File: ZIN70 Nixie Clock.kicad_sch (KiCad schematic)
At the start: 21 parts, among them U1 HV5122, U2 HV5122, U3 CD40109BPW

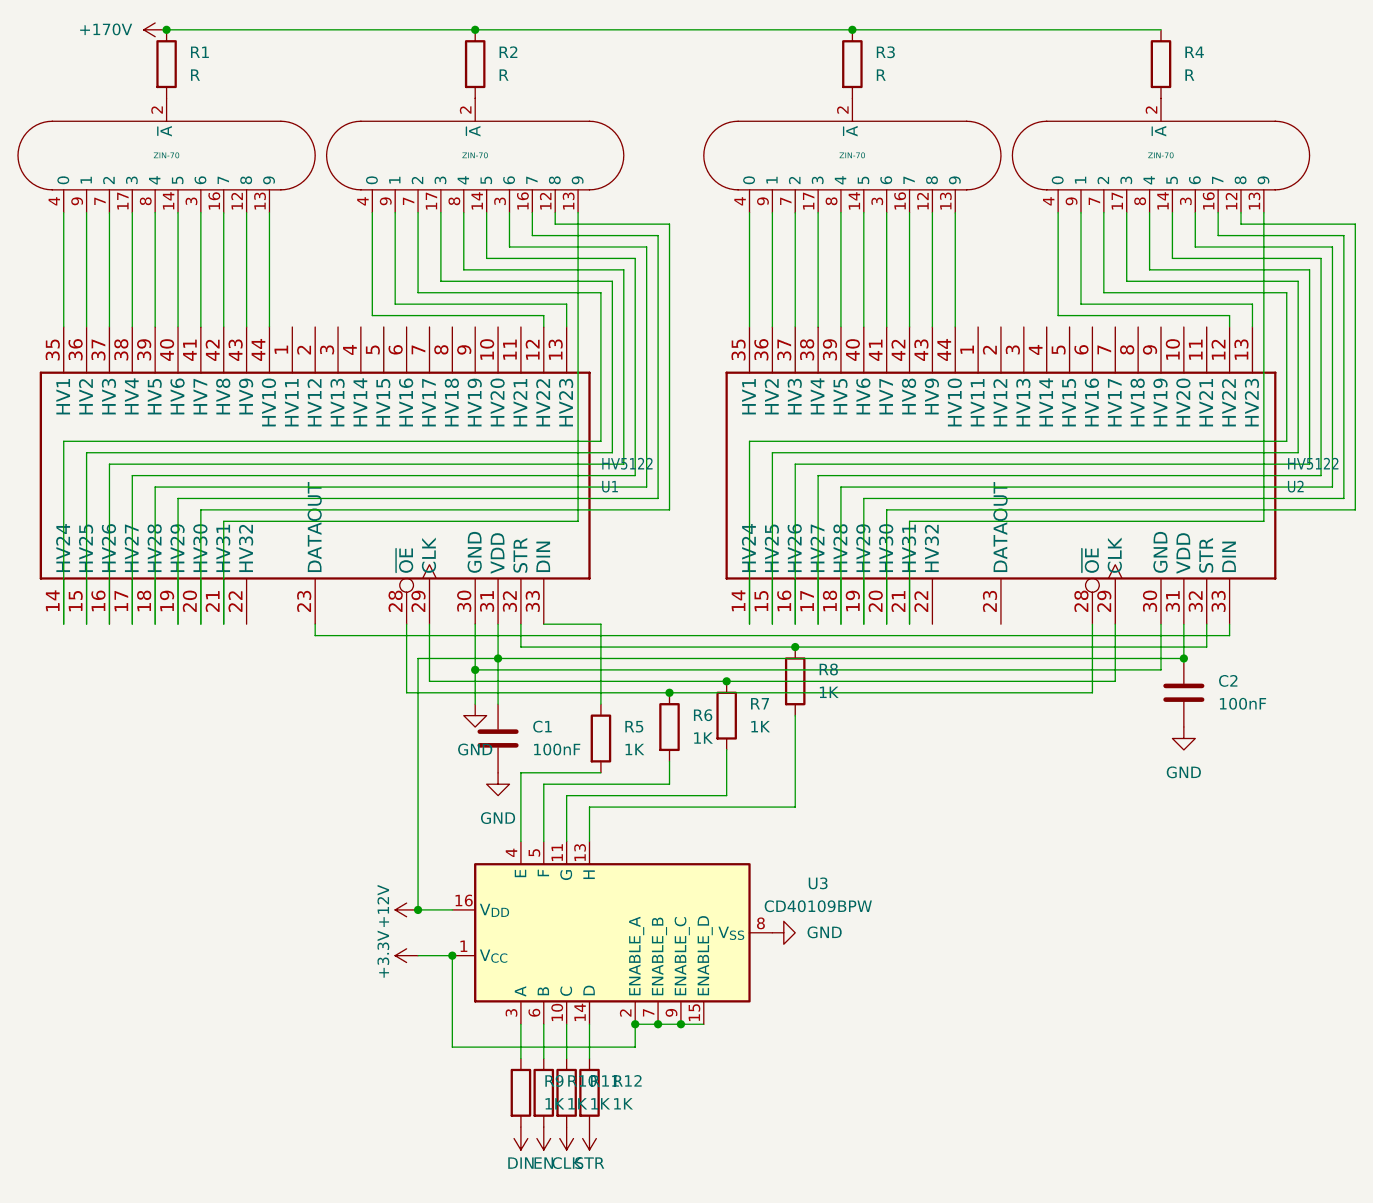
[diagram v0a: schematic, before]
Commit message: Update the clock with 5mm indicators
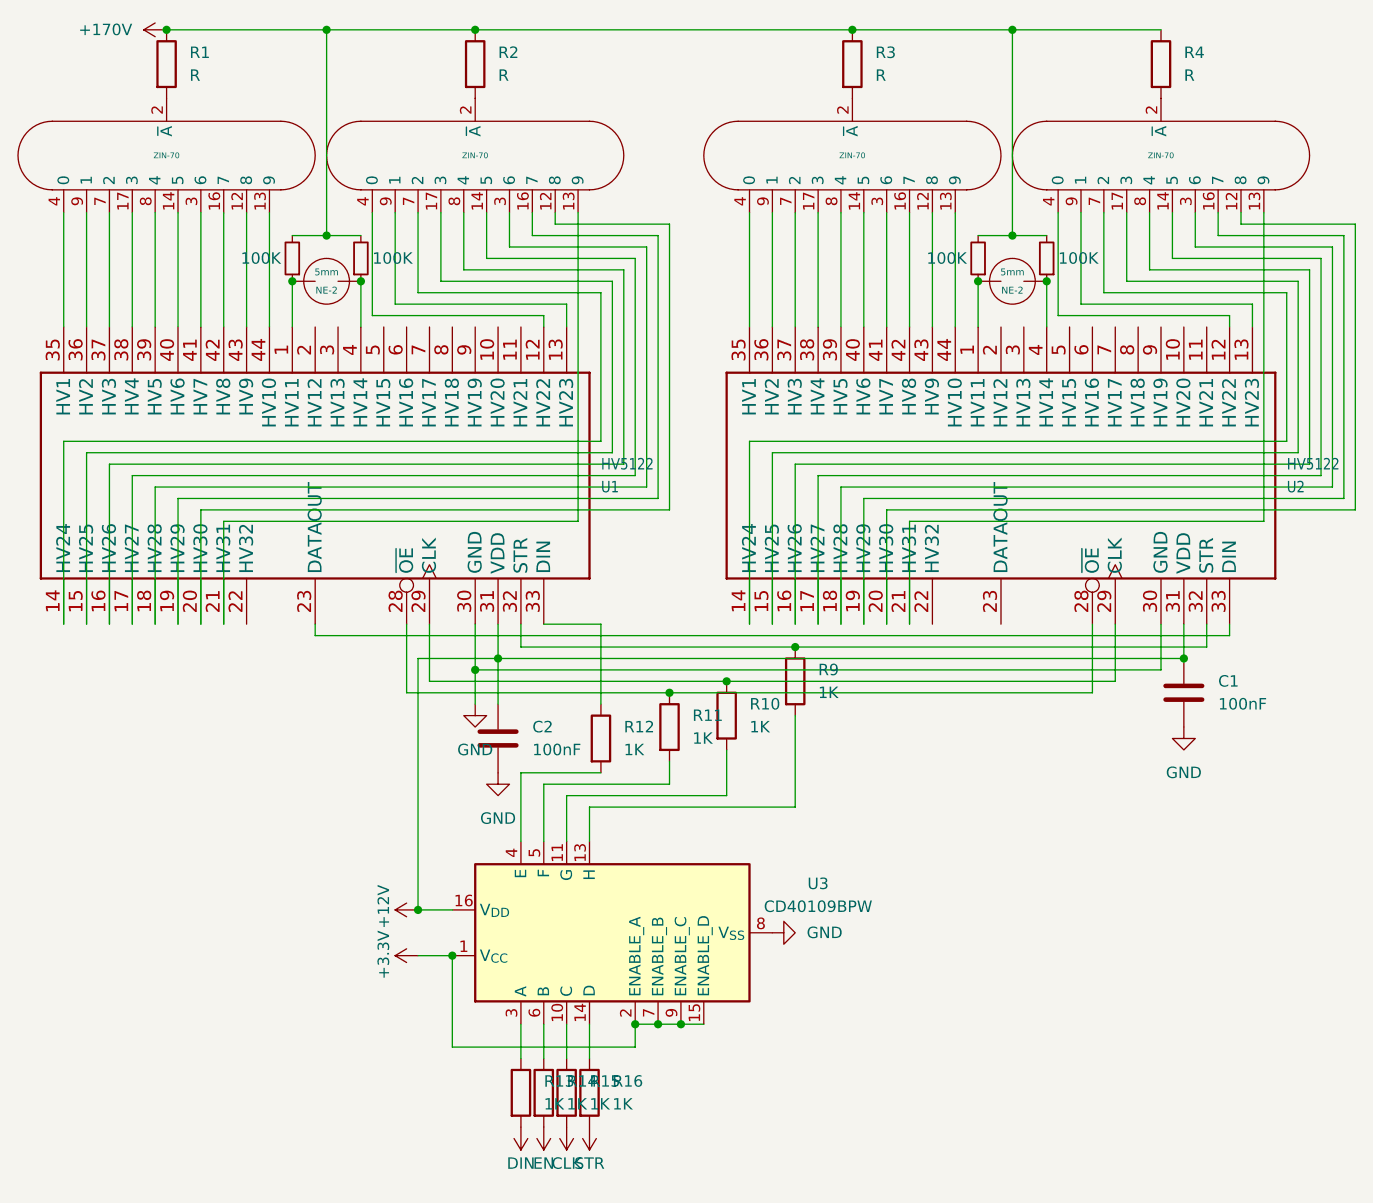
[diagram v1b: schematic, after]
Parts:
- added NE1, NE2: NE-2, NixFootprints:NE-2_5mm, symbol NixSymbols:NE-2_5mm
- added R5, R6, R7, R8: 100K, symbol Device:R_Small
- renumbered C2 to C1, C1 to C2, R7 to R10, R6 to R11, R5 to R12, R9 to R13, R10 to R14, R11 to R15, R12 to R16, R8 to R9
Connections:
- net +170V: now also R5.2, R6.2, R7.2, R8.2
- net at U2.1 (HV11): now also NE2., R7.1
- net at U2.4 (HV14): now also NE2., R8.1
- net at U1.1 (HV11): now also NE1., R5.1
- net at U1.4 (HV14): now also NE1., R6.1

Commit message: Major changes to design
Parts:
- added U4: LM78M05_TO220, Package_TO_SOT_THT:TO-220-3_Vertical, symbol Regulator_Linear:LM78M05_TO220
- R1, R2, R3, R4: value R -> 6.8K
- R5, R6, R7, R8: value 100K -> 200K
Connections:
- net +12V: now also U4.1 (VI)
- net GND: now also U4.2 (GND)
- new net +5V: U4.3 (VO)
